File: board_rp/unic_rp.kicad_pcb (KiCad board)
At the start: 4 copper layers, 50 x 15.2 mm, 193 parts, among them J1 SM03B-SRSS-TB, P1 USB_C_Plug_USB2.0, Q1 2N7002, Q10 2N7002, Q11 2N7002, Q12 2N7002, Q13 2N7002, Q14 2N7002, Q15 2N7002, Q16 2N7002, Q17 2N7002, Q18 2N7002, Q19 2N7002, Q2 2N7002, Q20 2N7002, Q21 2N7002, Q22 2N7002, Q23 2N7002, Q24 2N7002, Q25 2N7002, Q26 2N7002, Q27 2N7002, Q28 2N7002, Q29 2N7002, Q3 2N7002, Q30 2N7002, Q31 2N7002, Q32 2N7002, Q33 2N7002, Q34 2N7002, Q35 2N7002, Q36 2N7002, Q37 2N7002, Q38 2N7002, Q39 2N7002, Q4 2N7002, Q40 2N7002, Q41 2N7002, Q5 2N7002, Q6 2N7002, Q7 2N7002, Q8 2N7002, Q9 2N7002, U1 RP2350_80QFN, U3 MIC5203-3.3BM5, U4 APS6404L-3SQR-ZR, U6 AP62150Z6, U7 W25Q16JVUXIQ, X1 27MHz

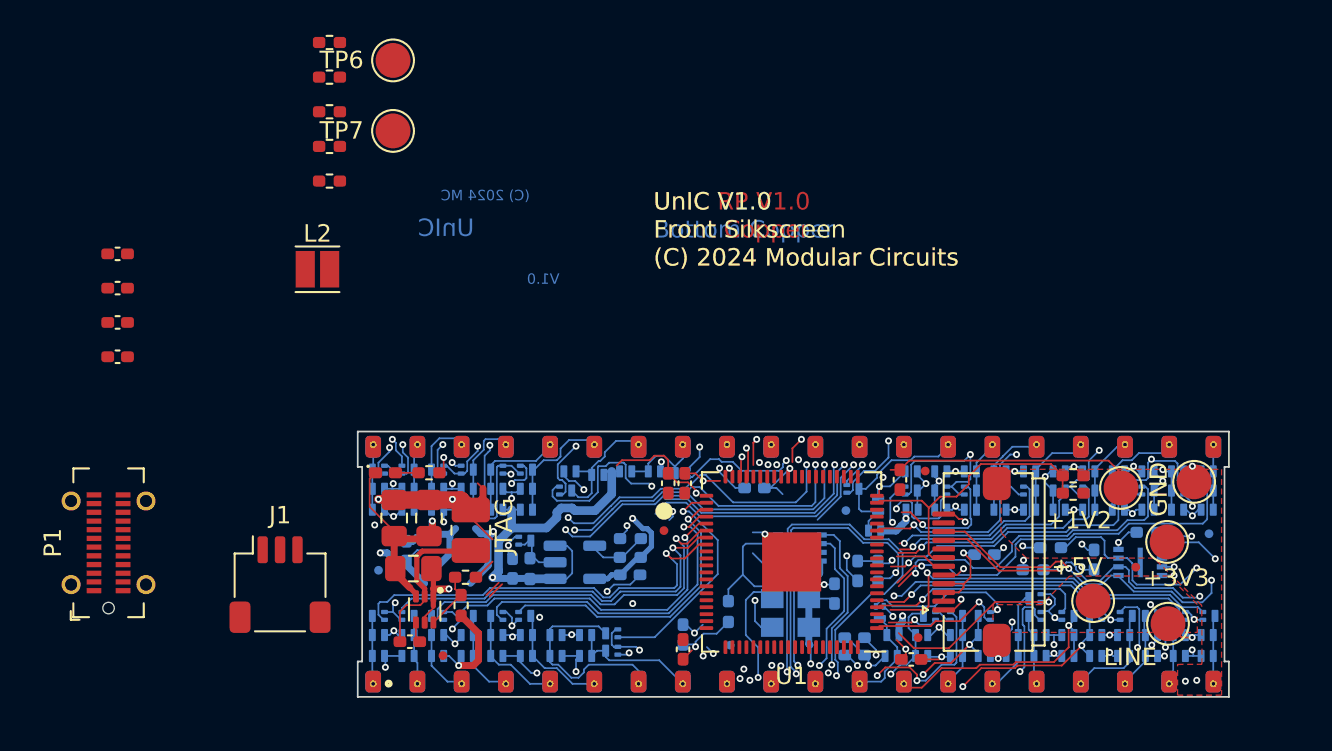
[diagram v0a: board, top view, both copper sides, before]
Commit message: More work towards RP based UnIC
The IO connections are mostly figured out, component placement
as well. Still need new inductor, proper XTAL, USB and of course
a lot of routing, including power.
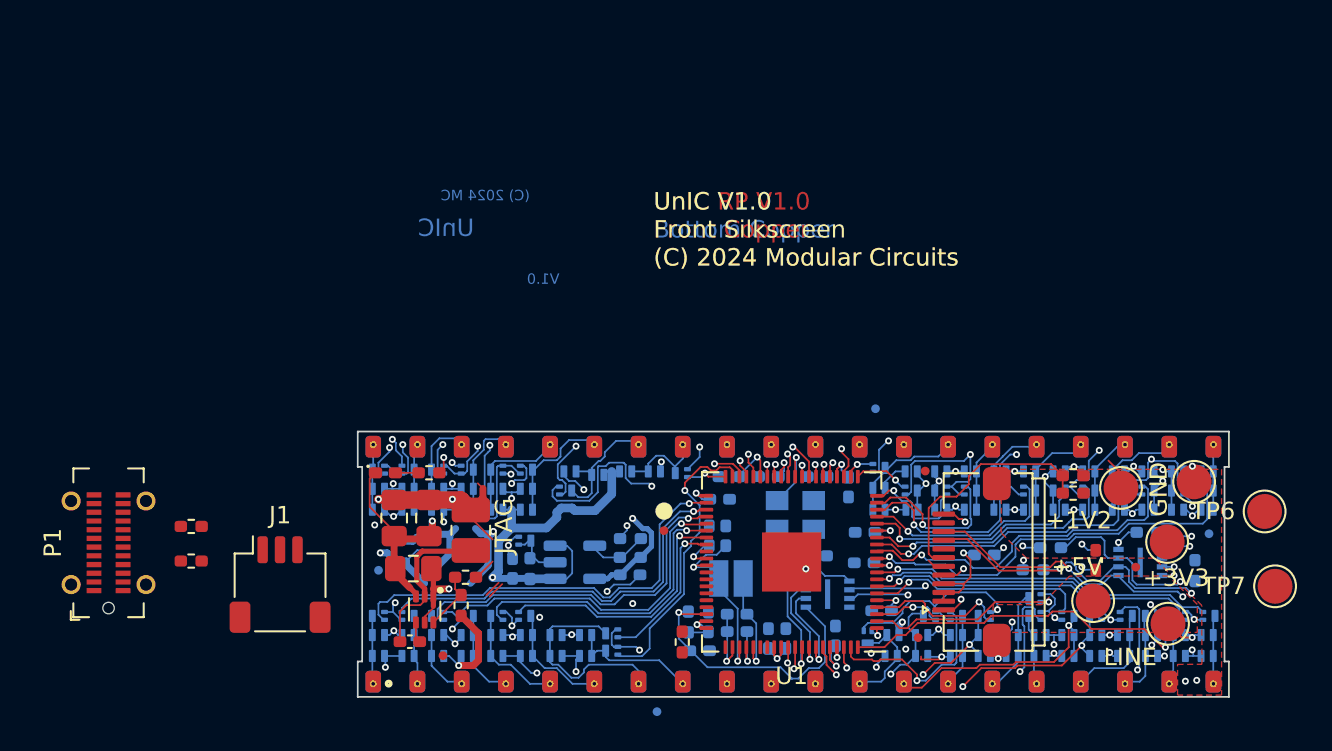
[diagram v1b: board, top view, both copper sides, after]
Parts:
- C11, C12, C15, C18, C20, C23, C24, C26, L2, R20, R21: moved to B.Cu
- moved TP7 57.0 mm to (91.0, 64.0)
- moved TP6 56.4 mm to (90.4, 59.7)
- moved R21 54.5 mm to (86.4, 63.1), turned to 90 degrees
- moved C18 47.6 mm to (68.4, 65.4), turned to 180 degrees
- moved C12 41.2 mm to (60.1, 65.6), turned to 180 degrees
- moved C26 38.9 mm to (60.1, 66.6), turned to 180 degrees
- moved C24 38.4 mm to (57.9, 67.7), turned to 180 degrees
- moved R19 36.6 mm to (56.9, 67.2), turned to -90 degrees
- moved R20 29.8 mm to (59.6, 57.7)
- moved L2 29.7 mm to (59.7, 63.5), turned to 180 degrees
- moved R12 28.9 mm to (28.7, 60.5)
- moved R18 28.9 mm to (28.7, 62.5)
- moved C4 24.9 mm to (80.7, 62.5)
- moved C14 22.4 mm to (58.4, 66.0), turned to 90 degrees
- moved C10 18.2 mm to (59.1, 59.0), turned to 0 degrees
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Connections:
- TP4 pad 1: +1V2 -> +1V1
- U1 pad 1: /PIN24_F -> /PIN12_F
- U1 pad 11: /PIN20_F -> /PIN21_F
- U1 pad 12: /PIN9_F -> /PIN30_F
- U1 pad 13: /PIN10_F -> /PIN22_F
- U1 pad 14: /PIN15_F -> /PIN23_F
- U1 pad 16: /PIN14_F -> /PIN29_F
- U1 pad 17: /PIN16_F -> /PIN24_F
- U1 pad 18: /PIN17_F -> /PIN25_F
- U1 pad 19: /PIN18_F -> /PIN26_F
- U1 pad 2: /PIN29_F -> /PIN15_F
- U1 pad 20: /PIN12_F -> /PIN31_F
- U1 pad 21: /PIN19_F -> /PIN32_F
- U1 pad 22: /PIN36_F -> /PIN27_F
- U1 pad 23: /PIN27_F -> /PIN28_F
- U1 pad 25: /PIN39_F -> /PIN34_F
- U1 pad 26: /PIN38_F -> /PIN35_F
- U1 pad 27: /PIN40_F -> /PIN36_F
- U1 pad 28: /PIN37_F -> /PIN39_F
- U1 pad 3: /PIN23_F -> /PIN9_F
- U1 pad 36: /PIN28_F -> /PIN38_F
- U1 pad 37: /PIN33_F -> /PIN40_F
- U1 pad 38: /PIN34_F -> /PIN37_F
- U1 pad 39: /PIN35_F -> /PIN8_F
- U1 pad 4: /PIN22_F -> /PIN10_F
- U1 pad 40: /PIN8_F -> /PIN33_F
- U1 pad 42: /PIN7_F -> /PIN1_F
- U1 pad 43: /PIN6_F -> /PIN2_F
- U1 pad 44: /PIN5_F -> /PIN3_F
- U1 pad 46: /PIN3_F -> /PIN5_F
- U1 pad 47: /PIN2_F -> /PIN6_F
- U1 pad 48: /PIN1_F -> /PIN7_F
- U1 pad 6: /PIN21_F -> /PIN13_F
- U1 pad 7: /PIN30_F -> /PIN11_F
- U1 pad 77: /PIN31_F -> /PIN17_F
- U1 pad 78: /PIN26_F -> /PIN16_F
- U1 pad 79: /PIN32_F -> /PIN14_F
- U1 pad 8: /PIN11_F -> /PIN19_F
- U1 pad 80: /PIN25_F -> /PIN18_F
- U1 pad 9: /PIN13_F -> /PIN20_F
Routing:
- net (no net): track 93.4 -> 2.02 mm, vias 10 -> 0
- net /PIN8_F: track 0.69 -> 16.8 mm
- net +1V2: track 14.6 -> 0.00 mm
- net /SPI_MISO_IO1: track 52.0 -> 37.6 mm
- net +1V1: track 29.6 -> 40.7 mm, vias 5 -> 6
- net GND: track 79.2 -> 68.2 mm, vias 43 -> 35
- net /SPI_IO3: track 48.9 -> 38.4 mm, vias 2 -> 3
- net /PIN12_F: track 11.1 -> 0.91 mm, vias 2 -> 1
- net /PIN19_F: track 28.5 -> 19.2 mm, vias 2 -> 1
- net Net-(U1-GPIO40_ADC0): track 22.5 -> 13.3 mm, vias 2 -> 1
- net /PIN18_F: track 28.8 -> 21.1 mm, vias 2 -> 1
- net /SPI_IO2: track 45.9 -> 39.5 mm
- net /VREG_LX: track 0.00 -> 6.04 mm, vias 0 -> 1
- net /PSRAM_CS_N: track 11.2 -> 17.2 mm
- net /PIN16_F: track 21.9 -> 17.0 mm
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- added copper zone on In2.Cu, net +1V1
- removed copper zone on In2.Cu, net +1V2
- removed copper zone on In1.Cu, net +5V

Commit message: More work towards UnIC-RP. This time power supplies are cleaned up a bit.
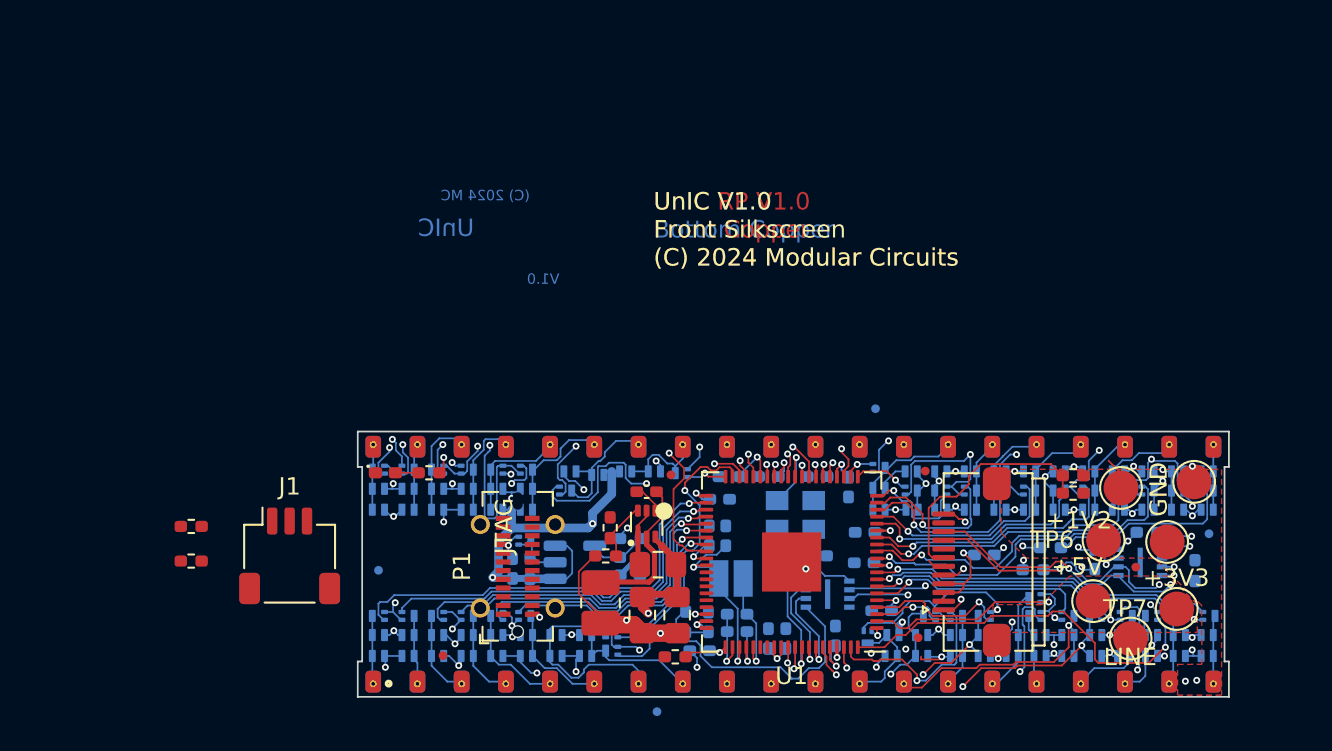
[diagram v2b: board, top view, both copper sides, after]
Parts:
- C4: moved to B.Cu
- moved P1 23.5 mm to (47.5, 62.8)
- moved C7 17.2 mm to (56.6, 65.6), turned to 90 degrees
- moved C6 16.1 mm to (54.9, 58.5), turned to 0 degrees
- moved C5 14.1 mm to (55.5, 62.7), turned to 0 degrees
- moved U6 13.7 mm to (54.9, 60.4), turned to 90 degrees
- moved C8 13.5 mm to (54.6, 65.6), turned to 90 degrees
- moved R5 9.65 mm to (52.8, 60.6), turned to 90 degrees
- moved TP6 9.40 mm to (81.1, 61.3)
- moved L1 8.54 mm to (52.2, 64.9), turned to -90 degrees
- moved R4 8.14 mm to (52.5, 62.2), turned to 0 degrees
- moved TP7 5.80 mm to (85.3, 65.3)
- moved FID8 3.22 mm to (56.3, 57.6)
- moved TP1 2.31 mm to (82.7, 67.0)
- moved J1 1.74 mm to (34.4, 62.2)
- moved R19 0.94 mm to (56.5, 68.0), turned to 0 degrees
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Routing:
- net GND: track 68.2 -> 52.3 mm, vias 35 -> 34
- net +1V1: track 40.7 -> 26.2 mm, vias 6 -> 4
- net /VREG_AVDD: track 0.00 -> 13.0 mm, vias 0 -> 2
- net Net-(U1-GPIO40_ADC0): track 13.3 -> 22.1 mm, vias 1 -> 2
- net /SPI_IO3: track 38.4 -> 30.3 mm
- net +3V3: track 47.0 -> 40.2 mm, vias 22 -> 19
- net +5V: track 81.3 -> 78.2 mm, vias 20 -> 19
- net /SPI_CLK: track 52.4 -> 49.5 mm
- net LINE: track 50.2 -> 47.7 mm
- net (no net): track 2.02 -> 0.00 mm
- net /PIN18_F: track 21.1 -> 22.4 mm
- net Net-(U6-BST): track 0.88 -> 1.72 mm
- net Net-(U6-SW): track 9.37 -> 8.82 mm
- net Net-(P1-GND-PadA1): vias 0 -> 1

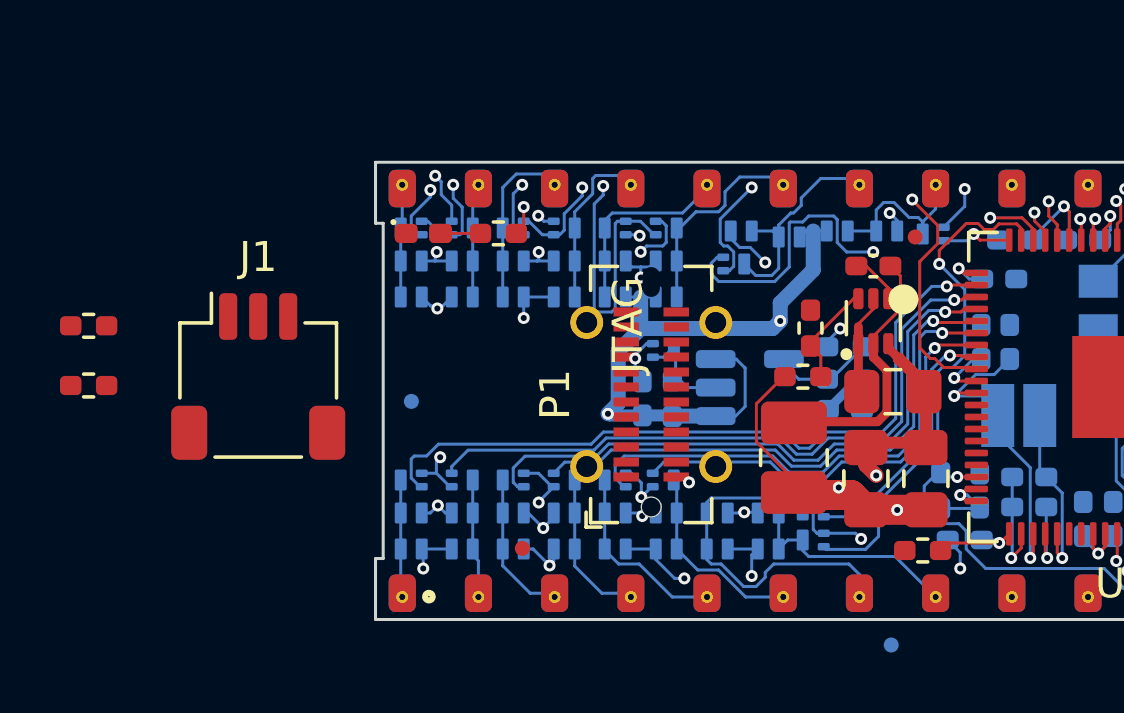
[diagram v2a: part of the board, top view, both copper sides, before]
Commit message: Much more complet RP schematic.
The USB-based debug setup is now drawn up. Component
placement is also complete. A thorough review is needed
especially on component footprints!
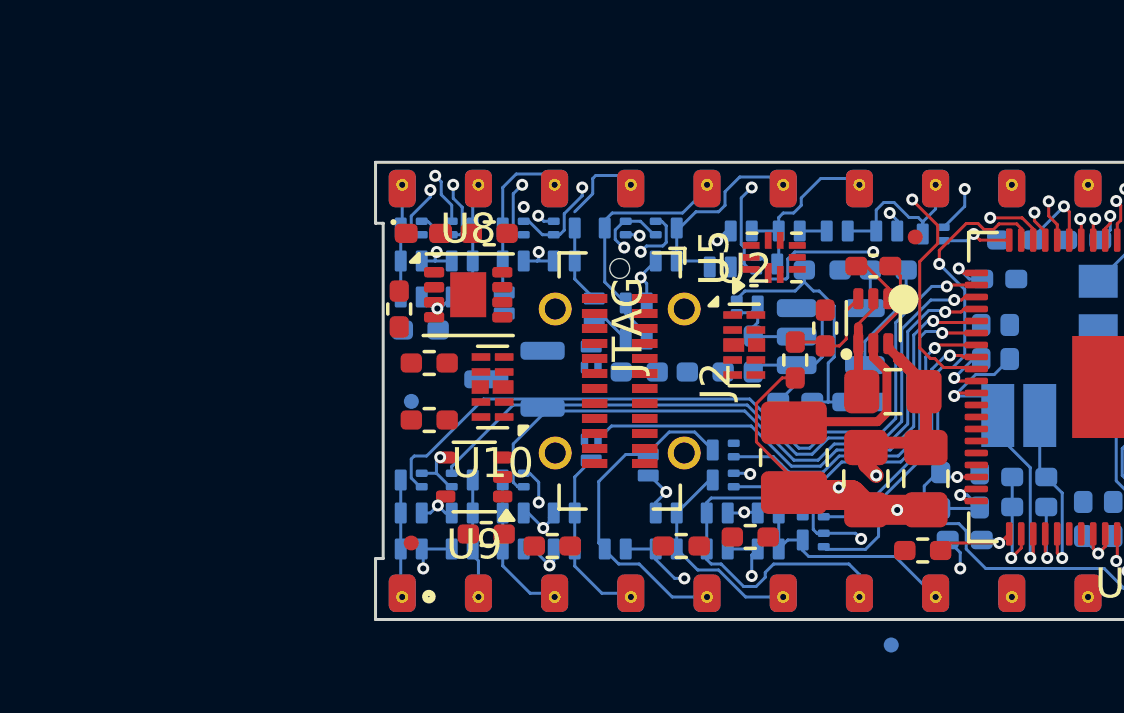
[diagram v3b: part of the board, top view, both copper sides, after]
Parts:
- removed J1: SM03B-SRSS-TB, Connector_JST:JST_SH_SM03B-SRSS-TB_1x03-1MP_P1.00mm_Horizontal
- removed P1: USB_C_Plug_USB2.0, Connector_USB:USB_C_Receptacle_GCT_USB4115-03-C
- added J2: USB_C_Receptacle, UNIC:USB_C_Receptacle_GCT_USB4115-03-C, F.Cu at (46.4, 62.4)
- added Q42: AO3401A, Package_TO_SOT_SMD:SOT-23, B.Cu at (42.9, 62.3)
- added Q43: 2N7002, UNIC:SOT-883, B.Cu at (45.5, 61.6)
- added R16: 10k, UNIC:R_0402_1005Metric_Pad0.72x0.64mm_HandSolder, B.Cu at (47.1, 62.1)
- added R22: 10k, UNIC:R_0402_1005Metric_Pad0.72x0.64mm_HandSolder, B.Cu at (49.3, 62.1)
- added R23: 10k, UNIC:R_0402_1005Metric_Pad0.72x0.64mm_HandSolder, F.Cu at (42.0, 67.5)
- added R24: 10k, UNIC:R_0402_1005Metric_Pad0.72x0.64mm_HandSolder, F.Cu at (44.2, 67.9)
- added R25: 5.1k, UNIC:R_0402_1005Metric_Pad0.72x0.64mm_HandSolder, B.Cu at (39.8, 60.7)
- added R26: 68.k, UNIC:R_0402_1005Metric_Pad0.72x0.64mm_HandSolder, F.Cu at (39.1, 60.0)
- added R6: 5.1k, UNIC:R_0402_1005Metric_Pad0.72x0.64mm_HandSolder, F.Cu at (40.1, 63.7)
- added R7: 5.1k, UNIC:R_0402_1005Metric_Pad0.72x0.64mm_HandSolder, F.Cu at (40.1, 61.8)
- added U10: ESD224DQA, Package_DFN_QFN:Diodes_UDFN-10_1.0x2.5mm_P0.5mm, F.Cu at (42.2, 62.6)
- added U2: ESD224DQA, Package_DFN_QFN:Diodes_UDFN-10_1.0x2.5mm_P0.5mm, F.Cu at (50.6, 61.2)
- added U5: TMUX154ERSW, Package_DFN_QFN:UQFN-10_1.4x1.8mm_P0.4mm, F.Cu at (51.6, 58.3)
- added U8: LM393, Package_SON:WSON-8-1EP_3x2.5mm_P0.5mm_EP1.2x1.5mm_PullBack, F.Cu at (41.4, 59.5)
- added U9: 74AUP1G08, Package_TO_SOT_SMD:SOT-353_SC-70-5, F.Cu at (41.6, 65.6)
- moved R12 23.1 mm to (50.8, 67.6), turned to 180 degrees
- moved R18 20.5 mm to (48.5, 67.9), turned to 180 degrees
- moved C1 5.10 mm to (52.3, 63.1), turned to 0 degrees
- moved R14 3.91 mm to (55.4, 58.7)
- moved Q8 3.74 mm to (49.9, 64.7)
- moved FID4 3.71 mm to (39.5, 67.8)
- moved U3 3.19 mm to (53.5, 60.9)
- moved Q41 3.16 mm to (50.7, 59.9)
- moved R17 3.08 mm to (50.9, 61.5)
- moved R15 2.68 mm to (53.2, 58.7)
- moved D51 2.06 mm to (49.8, 58.6), turned to 180 degrees
- moved Q7 2.00 mm to (49.9, 65.7), turned to 180 degrees
- moved D5 1.94 mm to (47.4, 65.2), turned to 90 degrees
- moved D50 1.57 mm to (47.0, 59.8)
- moved D49 1.57 mm to (47.0, 61.0), turned to 0 degrees
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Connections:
- R12 pad 2: unconnected-(R12-Pad2) -> /USB_DP
- R18 pad 2: unconnected-(R18-Pad2) -> /USB_DM
- U1 pad 52: unconnected-(U1-GPIO41_ADC1-Pad52) -> /USB_PWR_EN
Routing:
- net LINE: track 47.7 -> 33.7 mm, vias 21 -> 18
- net +5V: track 78.2 -> 71.0 mm
- net GND: track 52.3 -> 57.3 mm, vias 34 -> 32
- net /PIN5_F: track 17.1 -> 12.2 mm
- net /PIN5: track 6.39 -> 11.2 mm
- net /PIN34_F: track 22.2 -> 18.3 mm
- net /PIN6_F: track 14.6 -> 11.6 mm
- net /PIN36: track 6.40 -> 8.48 mm
- net /PIN34: track 7.40 -> 5.93 mm
- net /PIN3_F: track 20.8 -> 22.2 mm
- net Net-(LED_DONE1-A): track 1.33 -> 0.00 mm
- net /PIN4_F: track 18.5 -> 17.2 mm
- net Net-(U1-GPIO40_ADC0): track 22.1 -> 21.1 mm
- net /PIN2_F: track 22.3 -> 23.2 mm
- net /PIN1_F: track 24.7 -> 25.6 mm
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
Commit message: More work towards routing RP board.
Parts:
- moved Q3 9.36 mm to (52.2, 64.6)
- moved Q2 8.13 mm to (53.6, 65.4), turned to 180 degrees
- moved L2 1.13 mm to (60.6, 64.3)
- moved R22 0.98 mm to (48.4, 61.7), turned to 90 degrees
- moved R25 0.85 mm to (39.2, 61.3), turned to 90 degrees
- moved Q34 0.80 mm to (48.8, 57.3)
- moved R9 0.71 mm to (65.2, 62.7)
- moved C12 0.51 mm to (60.2, 66.1)
- moved C26 0.51 mm to (60.2, 67.1)
- moved FID5 0.43 mm to (39.4, 63.5)
- moved Q42 0.34 mm to (42.6, 62.3)
- moved U5 0.33 mm to (51.5, 58.6)
- moved Q43 0.30 mm to (45.2, 61.6), turned to -90 degrees
- moved R16 0.30 mm to (46.8, 62.1)
- moved R13 0.25 mm to (56.9, 66.0)
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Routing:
- net /USB_PWR_EN: track 0.00 -> 31.5 mm, vias 0 -> 1
- net Net-(U5-SEL): track 0.00 -> 25.6 mm
- net /USB_TXP: track 0.00 -> 22.1 mm, vias 0 -> 2
- net /USB_CC1: track 0.00 -> 20.6 mm, vias 0 -> 2
- net /USB_TXM: track 0.00 -> 20.0 mm, vias 0 -> 2
- net /LCD_CS_N: track 0.49 -> 17.4 mm, vias 0 -> 2
- net /VBUS: track 0.00 -> 16.6 mm, vias 0 -> 2
- net /LCD_RST_N: track 13.9 -> 30.2 mm, vias 0 -> 2
- net Net-(R24-Pad2): track 0.00 -> 15.4 mm, vias 0 -> 2
- net Net-(U1-USB_DM): track 0.00 -> 13.8 mm
- net /USB_DM: track 0.00 -> 13.7 mm, vias 0 -> 2
- net /PIN3_F: track 22.2 -> 9.63 mm
- net /SWCLK: track 0.73 -> 13.2 mm, vias 1 -> 2
- net /USB_DP: track 0.00 -> 12.0 mm
- net Net-(R23-Pad2): track 0.00 -> 12.0 mm
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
